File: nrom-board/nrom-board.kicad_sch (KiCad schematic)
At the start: 12 parts, among them J1 Cartridge Connector, SW1 SW_DIP_x04, SW2 SW_SPDT, U1 PRG ROM 512K, U2 CHR ROM 512K

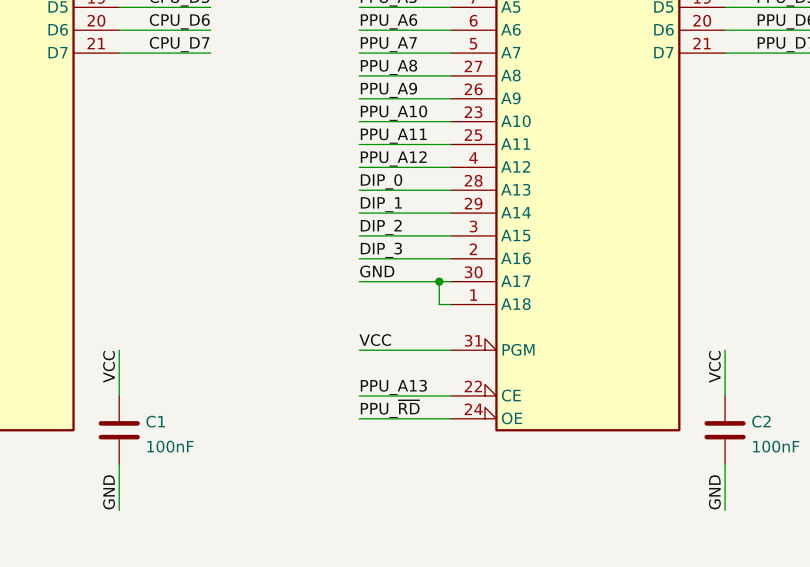
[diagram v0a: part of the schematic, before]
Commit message: NROM x16: Refactor ROM bankswitching circuit
- Refactor routing
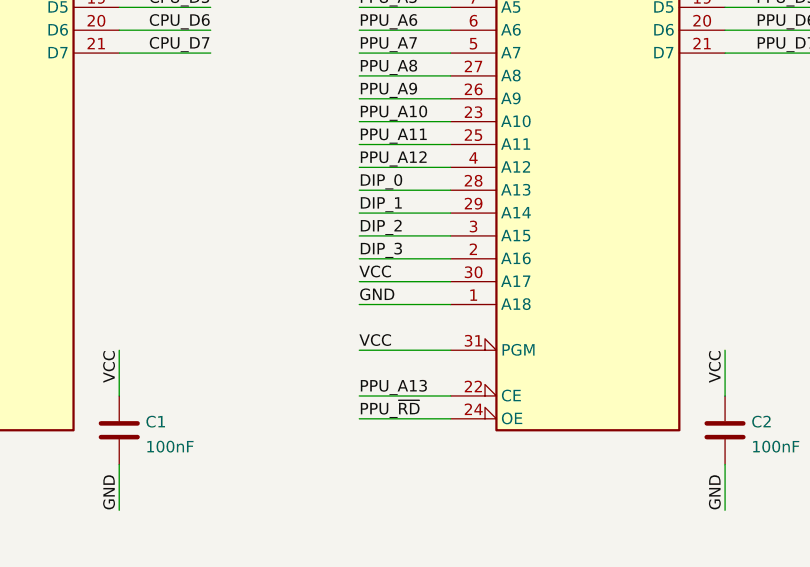
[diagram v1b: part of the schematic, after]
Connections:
- net GND: no longer U2.30 (A17)
- net VCC: now also U2.30 (A17)
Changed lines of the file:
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@@
   (title_block
     (title "FC NROM 256x16 Board")
-    (date "2022-09-05")
-    (rev "0.0.1")
+    (date "2022-11-25")
+    (rev "0.0.2")
     (company "Persune")
   )
@@
   (junction (at 213.36 142.24) (diameter 0) (color 0 0 0 0)
   )
-  (junction (at 153.67 69.85) (diameter 0) (color 0 0 0 0)
-  )
   (junction (at 19.05 25.4) (diameter 0) (color 0 0 0 0)
   )
@@
     (stroke (width 0) (type default) (color 0 0 0 0))
   )
-  (wire (pts (xy 153.67 69.85) (xy 154.94 69.85))
-    (stroke (width 0) (type default) (color 0 0 0 0))
-  )
   (wire (pts (xy 16.51 127) (xy 26.67 127))
     (stroke (width 0) (type default) (color 0 0 0 0))
@@
     (stroke (width 0) (type default) (color 0 0 0 0))
   )
-  (wire (pts (xy 154.94 72.39) (xy 153.67 72.39))
-    (stroke (width 0) (type default) (color 0 0 0 0))
-  )
   (wire (pts (xy 16.51 78.74) (xy 26.67 78.74))
     (stroke (width 0) (type default) (color 0 0 0 0))
@@
     (stroke (width 0) (type default) (color 0 0 0 0))
   )
+  (wire (pts (xy 144.78 72.39) (xy 154.94 72.39))
+    (stroke (width 0) (type default) (color 0 0 0 0))
+  )
   (wire (pts (xy 185.42 34.29) (xy 195.58 34.29))
     (stroke (width 0) (type default) (color 0 0 0 0))
   )
-  (wire (pts (xy 153.67 72.39) (xy 153.67 69.85))
-    (stroke (width 0) (type default) (color 0 0 0 0))
-  )
   (wire (pts (xy 39.37 132.08) (xy 49.53 132.08))
     (stroke (width 0) (type default) (color 0 0 0 0))
@@
     (stroke (width 0) (type default) (color 0 0 0 0))
   )
-  (wire (pts (xy 144.78 69.85) (xy 153.67 69.85))
-    (stroke (width 0) (type default) (color 0 0 0 0))
-  )
   (wire (pts (xy 20.32 27.94) (xy 21.59 27.94))
     (stroke (width 0) (type default) (color 0 0 0 0))
@@
     (stroke (width 0) (type default) (color 0 0 0 0))
   )
+  (wire (pts (xy 144.78 69.85) (xy 154.94 69.85))
+    (stroke (width 0) (type default) (color 0 0 0 0))
+  )
   (wire (pts (xy 16.51 88.9) (xy 26.67 88.9))
     (stroke (width 0) (type default) (color 0 0 0 0))
@@
     (effects (font (size 1.27 1.27)) (justify right bottom))
   )
+  (label "GND" (at 144.78 72.39 0)
+    (effects (font (size 1.27 1.27)) (justify left bottom))
+  )
   (label "GND" (at 218.44 142.24 180)
     (effects (font (size 1.27 1.27)) (justify right bottom))
@@
     (effects (font (size 1.27 1.27)) (justify right bottom))
   )
-  (label "GND" (at 144.78 69.85 0)
-    (effects (font (size 1.27 1.27)) (justify left bottom))
-  )
   (label "AUD_RF" (at 49.53 96.52 180)
     (effects (font (size 1.27 1.27)) (justify right bottom))
@@
     (effects (font (size 1.27 1.27)) (justify right bottom))
   )
+  (label "VCC" (at 144.78 69.85 0)
+    (effects (font (size 1.27 1.27)) (justify left bottom))
+  )
   (label "CPU_A13" (at 49.53 66.04 180)
